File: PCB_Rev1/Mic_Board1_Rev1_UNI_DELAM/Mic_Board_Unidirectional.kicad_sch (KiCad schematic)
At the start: 18 parts, among them J1 Conn_01x03_Pin, J2 532610771, U2 OPA1692xDGK

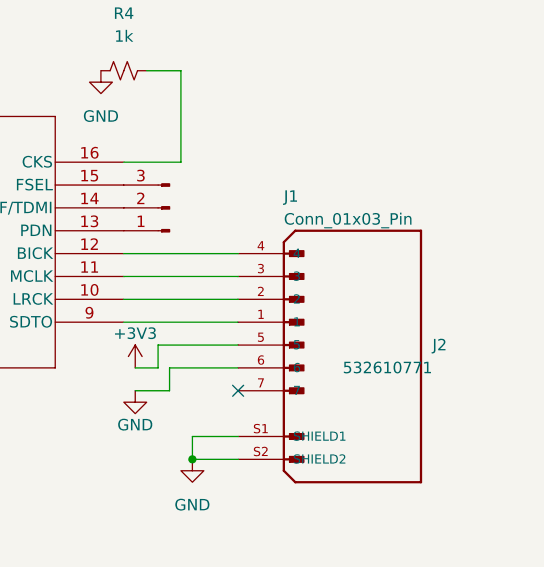
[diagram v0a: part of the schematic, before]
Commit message: MicBoard Added to MainBoard
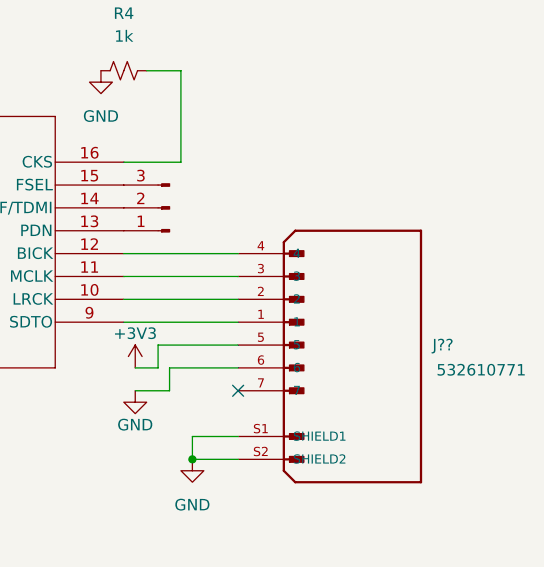
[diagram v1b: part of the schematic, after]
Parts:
- renumbered J2 to J??
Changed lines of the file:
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@@
 				)
 				(justify right)
+				(hide yes)
 			)
 		)
@@
 				)
 				(justify right)
+				(hide yes)
 			)
 		)
@@
 		(on_board yes)
 		(dnp no)
-		(property "Reference" "J2"
+		(property "Reference" "J??"
 			(at 252.73 113.03 0)
 			(effects
@@
 		)
 		(property "Value" "532610771"
-			(at 252.73 115.57 0)
+			(at 263.144 115.824 0)
 			(effects
 				(font
@@
 			(project "Mic_Board_Unidirectional"
 				(path "/1178ae07-c232-447f-a548-6d4f89d4abce"
-					(reference "J2")
+					(reference "J??")
 					(unit 1)
 				)

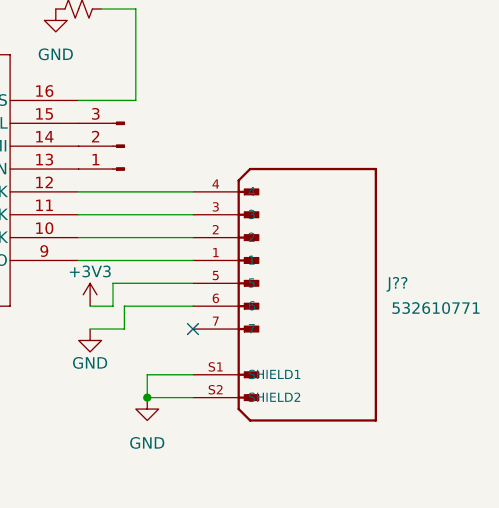
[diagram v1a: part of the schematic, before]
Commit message: Renamed J1 Connector MicBoard
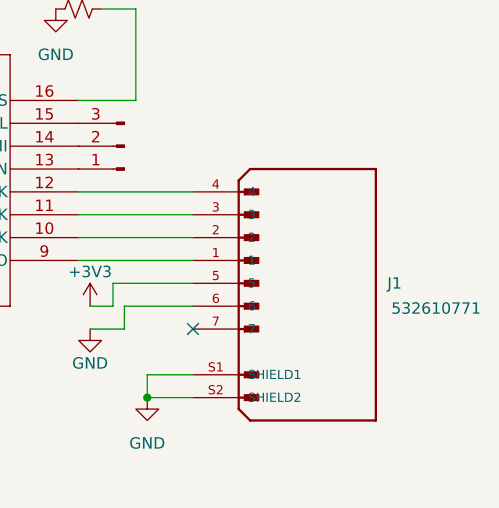
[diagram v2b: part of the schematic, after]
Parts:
- gave numbers to parts that had none: 1
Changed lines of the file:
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@@
 		(on_board yes)
 		(dnp no)
-		(property "Reference" "J??"
+		(property "Reference" "J1"
 			(at 252.73 113.03 0)
 			(effects
@@
 			(project "Mic_Board_Unidirectional"
 				(path "/1178ae07-c232-447f-a548-6d4f89d4abce"
-					(reference "J??")
+					(reference "J1")
 					(unit 1)
 				)

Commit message: Micboard pcb
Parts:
- removed J1: 532610771, cstar_mic_footprints:MOLEX_532610771, symbol 532610771:532610771
- removed MK1: Microphone, symbol Device:Microphone
- removed R1: 2.2K, symbol Device:R
- removed R2: 180k, symbol Device:R
- removed R3: 10k, symbol Device:R
- removed U1: ~, cstar_mic_footprints:SOIC_AK5720_AKM-L, symbol ADC:AK5720VT
- removed U2: OPA1692xDGK, Package_SO:VSSOP-8_3x3mm_P0.65mm, symbol Amplifier_Operational:OPA1692xDGK
- added C10: 1u, Capacitor_SMD:C_0805_2012Metric, symbol Device:C
- added C11: 0.47u, Capacitor_SMD:C_0805_2012Metric, symbol Device:C
- added C5: 10u, Capacitor_SMD:C_0805_2012Metric, symbol Device:C
- added J2: 532610771, Footprints:MOLEX_connector, symbol 532610771:532610771
- added MK1: CMC-97452-L100, Footprints:CONN_532610001-SD_02_MOL, symbol CMA-4544PF-W:CMA-4544PF-W
- added R1: 4.5k, Resistor_SMD:R_0805_2012Metric, symbol Device:R_Small_US
- added R2: 10k, Resistor_SMD:R_0805_2012Metric, symbol Device:R_Small_US
- added R3: 100k, Resistor_SMD:R_0805_2012Metric, symbol Device:R_Small_US
- added R5, R7: 1k, Resistor_SMD:R_0805_2012Metric, symbol Device:R_Small_US
- added R6: 9k, Resistor_SMD:R_0805_2012Metric, symbol Device:R_Small_US
- added TP2, TP3: TestPoint, TestPoint:TestPoint_Pad_D1.0mm, symbol Connector:TestPoint
- added U1: OPA1671IDBVR, Footprints:Op-Amp, symbol 2024-02-15_23-46-41:OPA1671IDBVR
- added U2: ~, Footprints:ADC, symbol ADC:AK5720VT
- C1: value 4.7u -> 1u; footprint (none) -> Capacitor_SMD:C_0805_2012Metric
- C2: value 0.47u -> 10u; footprint (none) -> Capacitor_SMD:C_0805_2012Metric
- C3: value 10u -> 500n
- C4: value 10u -> 80n
- C6, C7: value 1u -> 10u
- C9: value 0.47u -> 1u
- R4: value 1k -> 100k
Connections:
- net +3V3: now also C6.1, C8.2, C5.2, J2.5, R1.2, U1.5 (V+), U2.5 (VA), U2.6 (VD); no longer C3.2, C4.1, C6.2
- net GND: now also C1.2, C6.2, C8.1, TP1.1, C10.2, C11.2, C5.1, J2.6, J2.S1 (SHIELD1), J2.S2 (SHIELD2), MK1.2, R3.2, R7.1, U1.2 (V-), U2.4 (VSS); no longer C4.2, C6.1, C7.2, C8.2, R4.1
- net at C7.1: now also C4.2, R6.1, TP3.1, U1.1 (OUT)
- net at C9.1: now also U2.7 (GSEL)
- net at R4.2: now also C2.2, R3.1, TP2.1, U1.3 (+IN)
- net at C2.1: now also MK1.1, R2.2
- net at J1.1 (Pin_1): now also U2.13 (PDN)
- net at J1.2 (Pin_2): now also U2.14 (DIF/TDMI)
- net at J1.3 (Pin_3): now also U2.15 (FSEL)
- net at C1.1: now also R4.1, R1.1, R2.1
- new net: C4.1, R5.1, R6.2, U1.4 (-IN)
- new net: J2.1, U2.9 (SDTO)
- new net: J2.2, U2.10 (LRCK)
- new net: J2.3, U2.11 (MCLK)
- new net: J2.4, U2.12 (BICK)
- new net: C11.1, U2.1 (VCOM)
- new net: R7.2, U2.16 (CKS)
- new net: C7.2, U2.2 (RIN), U2.3 (LIN)
- new net: C10.1, U2.8 (REGO)
- new net: C3.2, R5.2

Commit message: Mounting holes?
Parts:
- added H1, H2, H3, H4: MountingHole, MountingHole:MountingHole_3.2mm_M3, symbol Mechanical:MountingHole

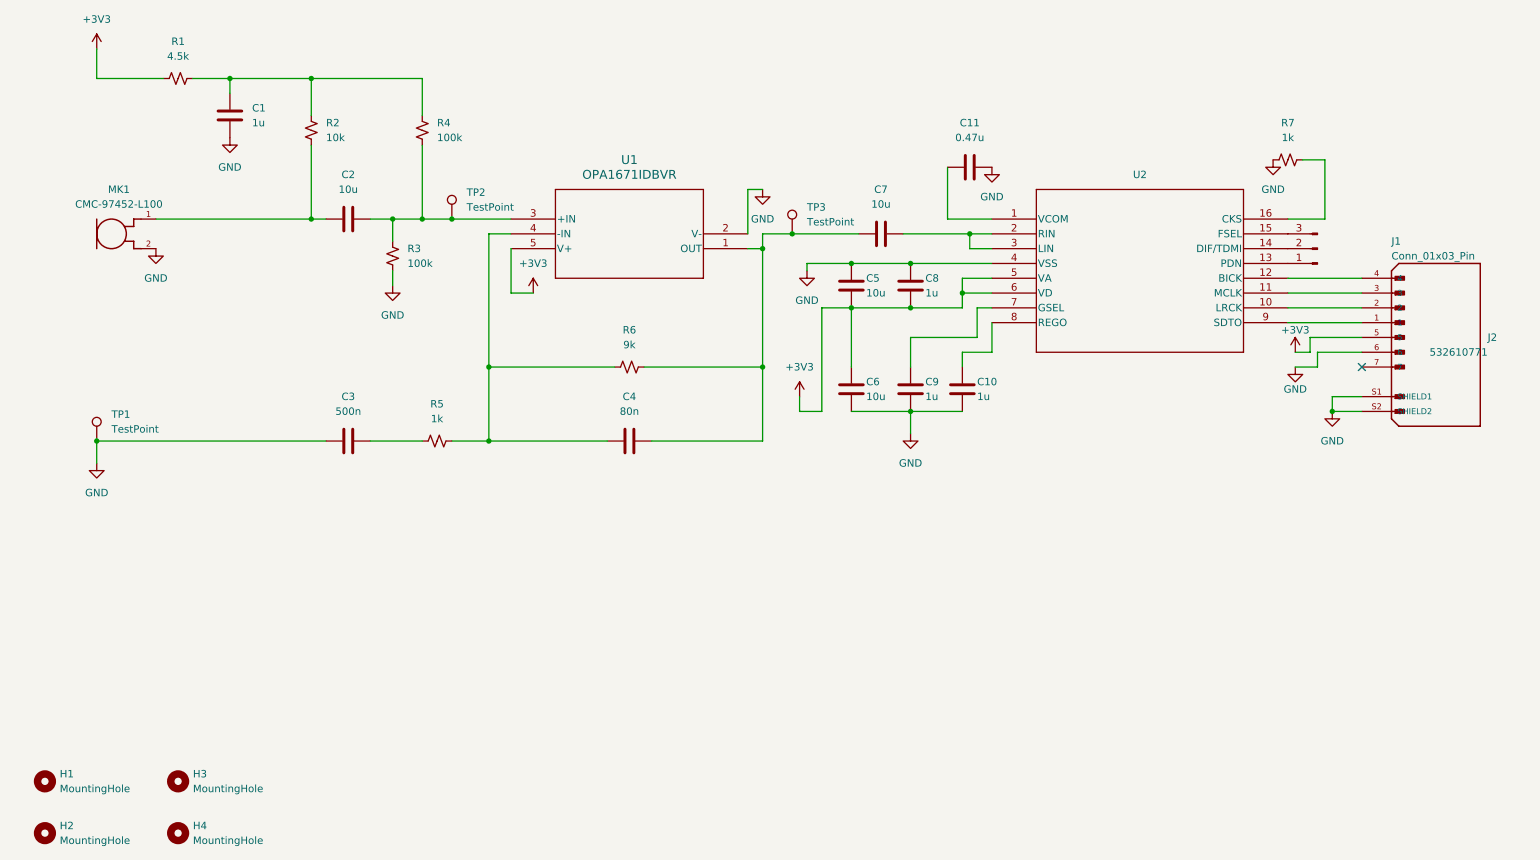
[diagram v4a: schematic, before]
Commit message: Mic Board Mounting Hole Placement + Fillets + Eliminating Errors
Placed mounting holes, added fillets to the corners of the pcb, and eliminated errors by using correct connector in place of the microphone in the schematic + layout
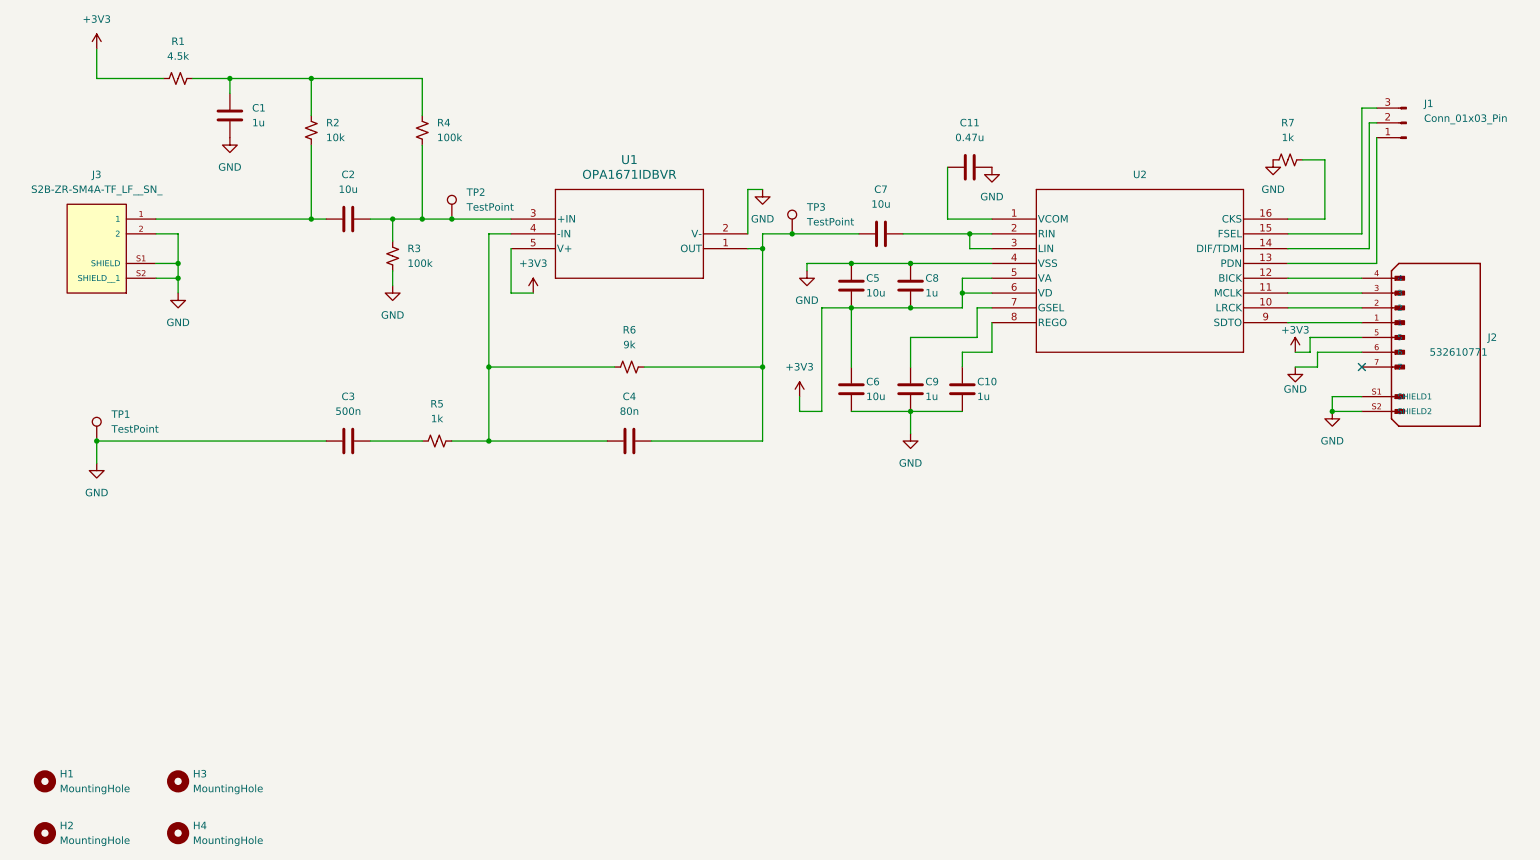
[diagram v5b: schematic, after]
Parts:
- removed MK1: CMC-97452-L100, Footprints:CONN_532610001-SD_02_MOL, symbol CMA-4544PF-W:CMA-4544PF-W
- added J3: S2B-ZR-SM4A-TF_LF__SN_, Footprints:Mic_Conn, symbol Mic Connectors:S2B-ZR-SM4A-TF_LF__SN_
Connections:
- net GND: now also J3.2, J3.S1 (SHIELD), J3.S2 (SHIELD__1)
- net at C2.1, R2.2: now also J3.1
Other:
- moved on the sheet: J1

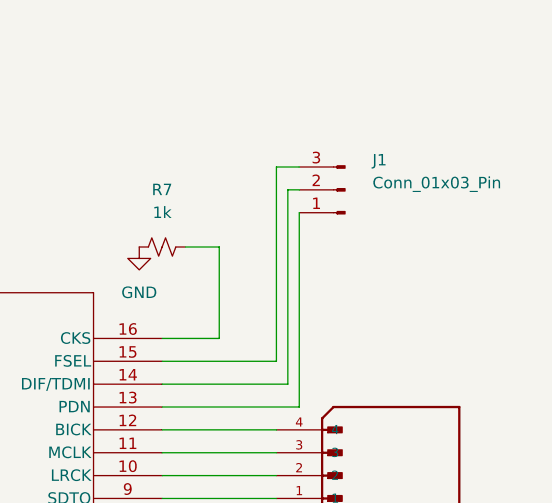
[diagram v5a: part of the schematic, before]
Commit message: Grounded Mic Board Mounting Holes
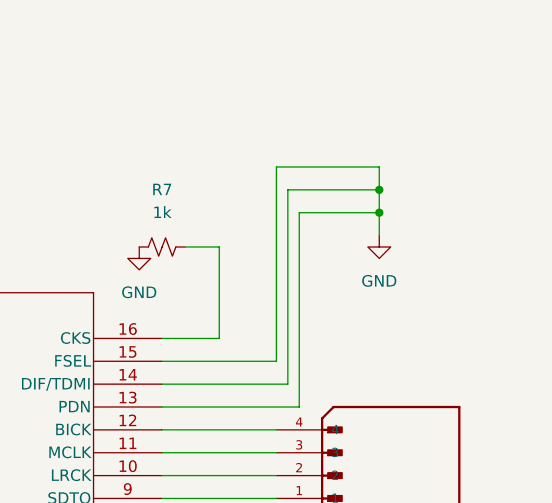
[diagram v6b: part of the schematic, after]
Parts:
- removed J1: Conn_01x03_Pin, Connector_PinHeader_2.54mm:PinHeader_1x03_P2.54mm_Vertical, symbol Connector:Conn_01x03_Pin
- H1, H2, H3, H4: footprint MountingHole:MountingHole_3.2mm_M3 -> MountingHole:MountingHole_3.2mm_M3_DIN965_Pad
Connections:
- net GND: now also U2.13 (PDN), U2.14 (DIF/TDMI), U2.15 (FSEL)
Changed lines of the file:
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@@
 	)
 	(junction
+		(at 259.08 67.31)
+		(diameter 0)
+		(color 0 0 0 0)
+	)
+	(junction
+		(at 259.08 69.85)
+		(diameter 0)
+		(color 0 0 0 0)
+	)
+	(junction
 		(at 179.07 96.52)
 		(diameter 0)
@@
 	(wire
 		(pts
+			(xy 259.08 64.77) (xy 259.08 67.31)
+		)
+		(stroke
+			(width 0)
+			(type default)
+		)
+	)
+	(wire
+		(pts
 			(xy 91.44 83.82) (xy 101.6 83.82)
 		)
@@
 	(wire
 		(pts
+			(xy 250.19 69.85) (xy 259.08 69.85)
+		)
+		(stroke
+			(width 0)
+			(type default)
+		)
+	)
+	(wire
+		(pts
 			(xy 101.6 96.52) (xy 101.6 88.9)
 		)
@@
 	(wire
 		(pts
+			(xy 259.08 67.31) (xy 259.08 69.85)
+		)
+		(stroke
+			(width 0)
+			(type default)
+		)
+	)
+	(wire
+		(pts
 			(xy 86.36 71.12) (xy 86.36 83.82)
 		)
@@
 	(wire
 		(pts
-			(xy 250.19 64.77) (xy 247.65 64.77)
+			(xy 259.08 69.85) (xy 259.08 72.39)
+		)
+		(stroke
+			(width 0)
+			(type default)
+		)
+	)
+	(wire
+		(pts
+			(xy 247.65 64.77) (xy 259.08 64.77)
 		)
 		(stroke
@@
 	(wire
 		(pts
-			(xy 250.19 67.31) (xy 248.92 67.31)
+			(xy 248.92 67.31) (xy 259.08 67.31)
 		)
 		(stroke
@@
 			)
 		)
-		(property "Footprint" "MountingHole:MountingHole_3.2mm_M3"
+		(property "Footprint" "MountingHole:MountingHole_3.2mm_M3_DIN965_Pad"
 			(at 21.59 189.23 0)
 			(effects
@@
 	)
 	(symbol
-		(lib_id "Connector:Conn_01x03_Pin")
-		(at 255.27 67.31 180)
-		(unit 1)
-		(exclude_from_sim no)
-		(in_bom yes)
-		(on_board yes)
-		(dnp no)
-		(property "Reference" "J1"
-			(at 258.318 64.008 0)
-			(effects
-				(font
-					(size 1.27 1.27)
-				)
-				(justify right)
-			)
-		)
-		(property "Value" "Conn_01x03_Pin"
-			(at 258.318 66.548 0)
-			(effects
-				(font
-					(size 1.27 1.27)
-				)
-				(justify right)
-			)
-		)
-		(property "Footprint" "Connector_PinHeader_2.54mm:PinHeader_1x03_P2.54mm_Vertical"
-			(at 255.27 67.31 0)
-			(effects
-				(font
-					(size 1.27 1.27)
-				)
-				(hide yes)
-			)
-		)
-		(property "Datasheet" "~"
-			(at 255.27 67.31 0)
-			(effects
-				(font
-					(size 1.27 1.27)
-				)
-				(hide yes)
-			)
-		)
-		(property "Description" ""
-			(at 255.27 67.31 0)
-			(effects
-				(font
-					(size 1.27 1.27)
-				)
-				(hide yes)
-			)
-		)
-		(pin "1"
-		)
-		(pin "2"
-		)
-		(pin "3"
-		)
-		(instances
-			(project "Mic_Board_Unidirectional"
-				(path "/1178ae07-c232-447f-a548-6d4f89d4abce"
-					(reference "J1")
-					(unit 1)
-				)
-			)
-		)
-	)
-	(symbol
 		(lib_id "Device:C")
 		(at 53.34 66.04 0)
@@
 			)
 		)
-		(property "Footprint" "MountingHole:MountingHole_3.2mm_M3"
+		(property "Footprint" "MountingHole:MountingHole_3.2mm_M3_DIN965_Pad"
 			(at 44.45 189.23 0)
 			(effects
@@
 			)
 		)
-		(property "Footprint" "MountingHole:MountingHole_3.2mm_M3"
+		(property "Footprint" "MountingHole:MountingHole_3.2mm_M3_DIN965_Pad"
 			(at 44.45 180.34 0)
 			(effects
@@
 	)
 	(symbol
+		(lib_id "power:GND")
+		(at 259.08 72.39 0)
+		(unit 1)
+		(exclude_from_sim no)
+		(in_bom yes)
+		(on_board yes)
+		(dnp no)
+		(fields_autoplaced yes)
+		(property "Reference" "#PWR01"
+			(at 259.08 78.74 0)
+			(effects
+				(font
+					(size 1.27 1.27)
+				)
+				(hide yes)
+			)
+		)
+		(property "Value" "GND"
+			(at 259.08 77.47 0)
+			(effects
+				(font
+					(size 1.27 1.27)
+				)
+			)
+		)
+		(property "Footprint" ""
+			(at 259.08 72.39 0)
+			(effects
+				(font
+					(size 1.27 1.27)
+				)
+				(hide yes)
+			)
+		)
+		(property "Datasheet" ""
+			(at 259.08 72.39 0)
+			(effects
+				(font
+					(size 1.27 1.27)
+				)
+				(hide yes)
+			)
+		)
+		(property "Description" "Power symbol creates a global label with name \"GND\" , ground"
+			(at 259.08 72.39 0)
+			(effects
+				(font
+					(size 1.27 1.27)
+				)
+				(hide yes)
+			)
+		)
+		(pin "1"
+		)
+		(instances
+			(project ""
+				(path "/1178ae07-c232-447f-a548-6d4f89d4abce"
+					(reference "#PWR01")
+					(unit 1)
+				)
+			)
+		)
+	)
+	(symbol
 		(lib_id "power:+3V3")
 		(at 236.22 106.68 0)
@@
 			)
 		)
-		(property "Footprint" "MountingHole:MountingHole_3.2mm_M3"
+		(property "Footprint" "MountingHole:MountingHole_3.2mm_M3_DIN965_Pad"
 			(at 21.59 180.34 0)
 			(effects

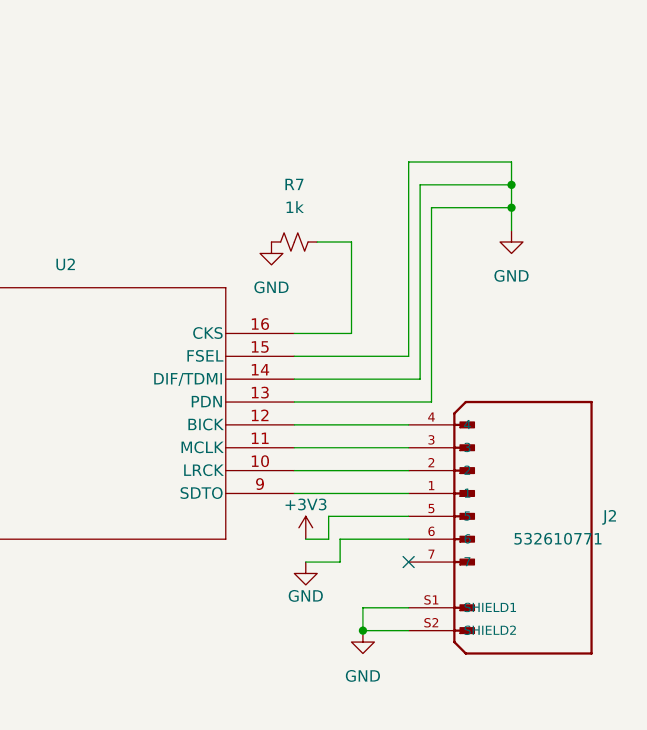
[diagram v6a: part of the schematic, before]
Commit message: Audio Connector Pins
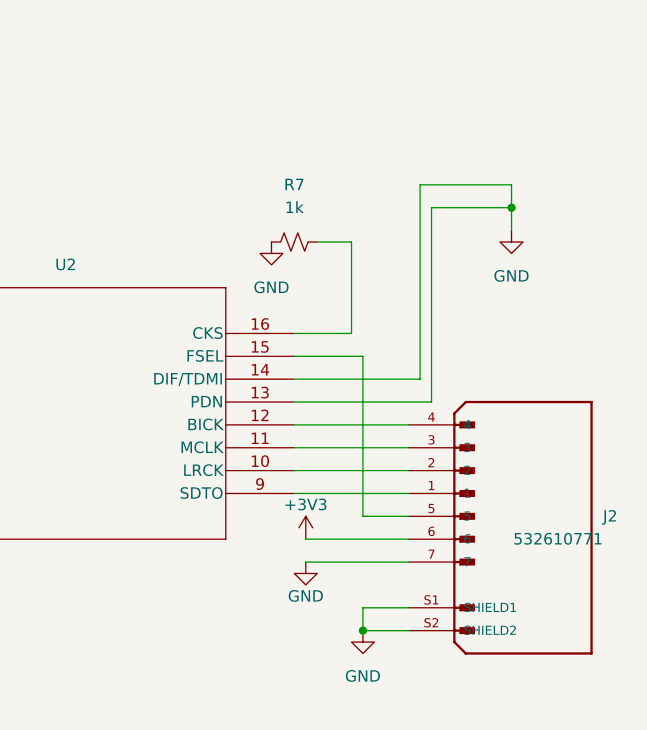
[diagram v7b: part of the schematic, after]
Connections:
- net +3V3: now also J2.6; no longer J2.5
- net GND: now also J2.7; no longer J2.6, U2.15 (FSEL)
- new net: J2.5, U2.15 (FSEL)
- no-connect marks 1 -> 0
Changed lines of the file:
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@@
-	)
-	(junction
-		(at 259.08 67.31)
-		(diameter 0)
-		(color 0 0 0 0)
 	)
 	(junction
@@
 		(color 0 0 0 0)
 	)
-	(no_connect
-		(at 247.65 109.22)
-	)
 	(wire
 		(pts
@@
 	(wire
 		(pts
-			(xy 259.08 64.77) (xy 259.08 67.31)
-		)
-		(stroke
-			(width 0)
-			(type default)
-		)
-	)
-	(wire
-		(pts
 			(xy 91.44 83.82) (xy 101.6 83.82)
 		)
@@
 	(wire
 		(pts
+			(xy 242.57 86.36) (xy 242.57 104.14)
+		)
+		(stroke
+			(width 0)
+			(type default)
+		)
+	)
+	(wire
+		(pts
 			(xy 144.78 121.92) (xy 144.78 109.22)
 		)
@@
 	(wire
 		(pts
-			(xy 236.22 106.68) (xy 238.76 106.68)
+			(xy 236.22 106.68) (xy 247.65 106.68)
 		)
 		(stroke
@@
 	(wire
 		(pts
+			(xy 234.95 86.36) (xy 242.57 86.36)
+		)
+		(stroke
+			(width 0)
+			(type default)
+		)
+	)
+	(wire
+		(pts
 			(xy 176.53 74.93) (xy 176.53 83.82)
 		)
@@
 	(wire
 		(pts
-			(xy 240.03 109.22) (xy 240.03 106.68)
-		)
-		(stroke
-			(width 0)
-			(type default)
-		)
-	)
-	(wire
-		(pts
 			(xy 40.64 86.36) (xy 44.45 86.36)
 		)
@@
 	(wire
 		(pts
-			(xy 247.65 86.36) (xy 234.95 86.36)
-		)
-		(stroke
-			(width 0)
-			(type default)
-		)
-	)
-	(wire
-		(pts
 			(xy 86.36 83.82) (xy 91.44 83.82)
 		)
@@
 	(wire
 		(pts
-			(xy 240.03 106.68) (xy 247.65 106.68)
-		)
-		(stroke
-			(width 0)
-			(type default)
-		)
-	)
-	(wire
-		(pts
 			(xy 142.24 88.9) (xy 144.78 88.9)
 		)
@@
 	(wire
 		(pts
-			(xy 236.22 109.22) (xy 240.03 109.22)
+			(xy 236.22 109.22) (xy 247.65 109.22)
+		)
+		(stroke
+			(width 0)
+			(type default)
+		)
+	)
+	(wire
+		(pts
+			(xy 242.57 104.14) (xy 247.65 104.14)
 		)
 		(stroke
@@
 	(wire
 		(pts
-			(xy 238.76 104.14) (xy 247.65 104.14)
-		)
-		(stroke
-			(width 0)
-			(type default)
-		)
-	)
-	(wire
-		(pts
 			(xy 152.4 91.44) (xy 160.02 91.44)
 		)
@@
 	(wire
 		(pts
-			(xy 247.65 64.77) (xy 247.65 86.36)
-		)
-		(stroke
-			(width 0)
-			(type default)
-		)
-	)
-	(wire
-		(pts
 			(xy 168.91 86.36) (xy 180.34 86.36)
 		)
@@
 	(wire
 		(pts
-			(xy 238.76 106.68) (xy 238.76 104.14)
-		)
-		(stroke
-			(width 0)
-			(type default)
-		)
-	)
-	(wire
-		(pts
 			(xy 44.45 91.44) (xy 44.45 93.98)
 		)
@@
 		)
 		(stroke
-			(width 0)
-			(type default)
-		)
-	)
-	(wire
-		(pts
-			(xy 247.65 64.77) (xy 259.08 64.77)
-		)
-		(stroke
